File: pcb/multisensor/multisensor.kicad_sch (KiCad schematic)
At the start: 20 parts, among them J1 TTL_Serial, J2 mmWave_Data, J3 mmWave_Support, J4 PIR_Sensor, J5 BME680, J6 BH1750, J7 USB_B_Micro, Q1 PN2222A, Q2 PN2222A, SW1 RESET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

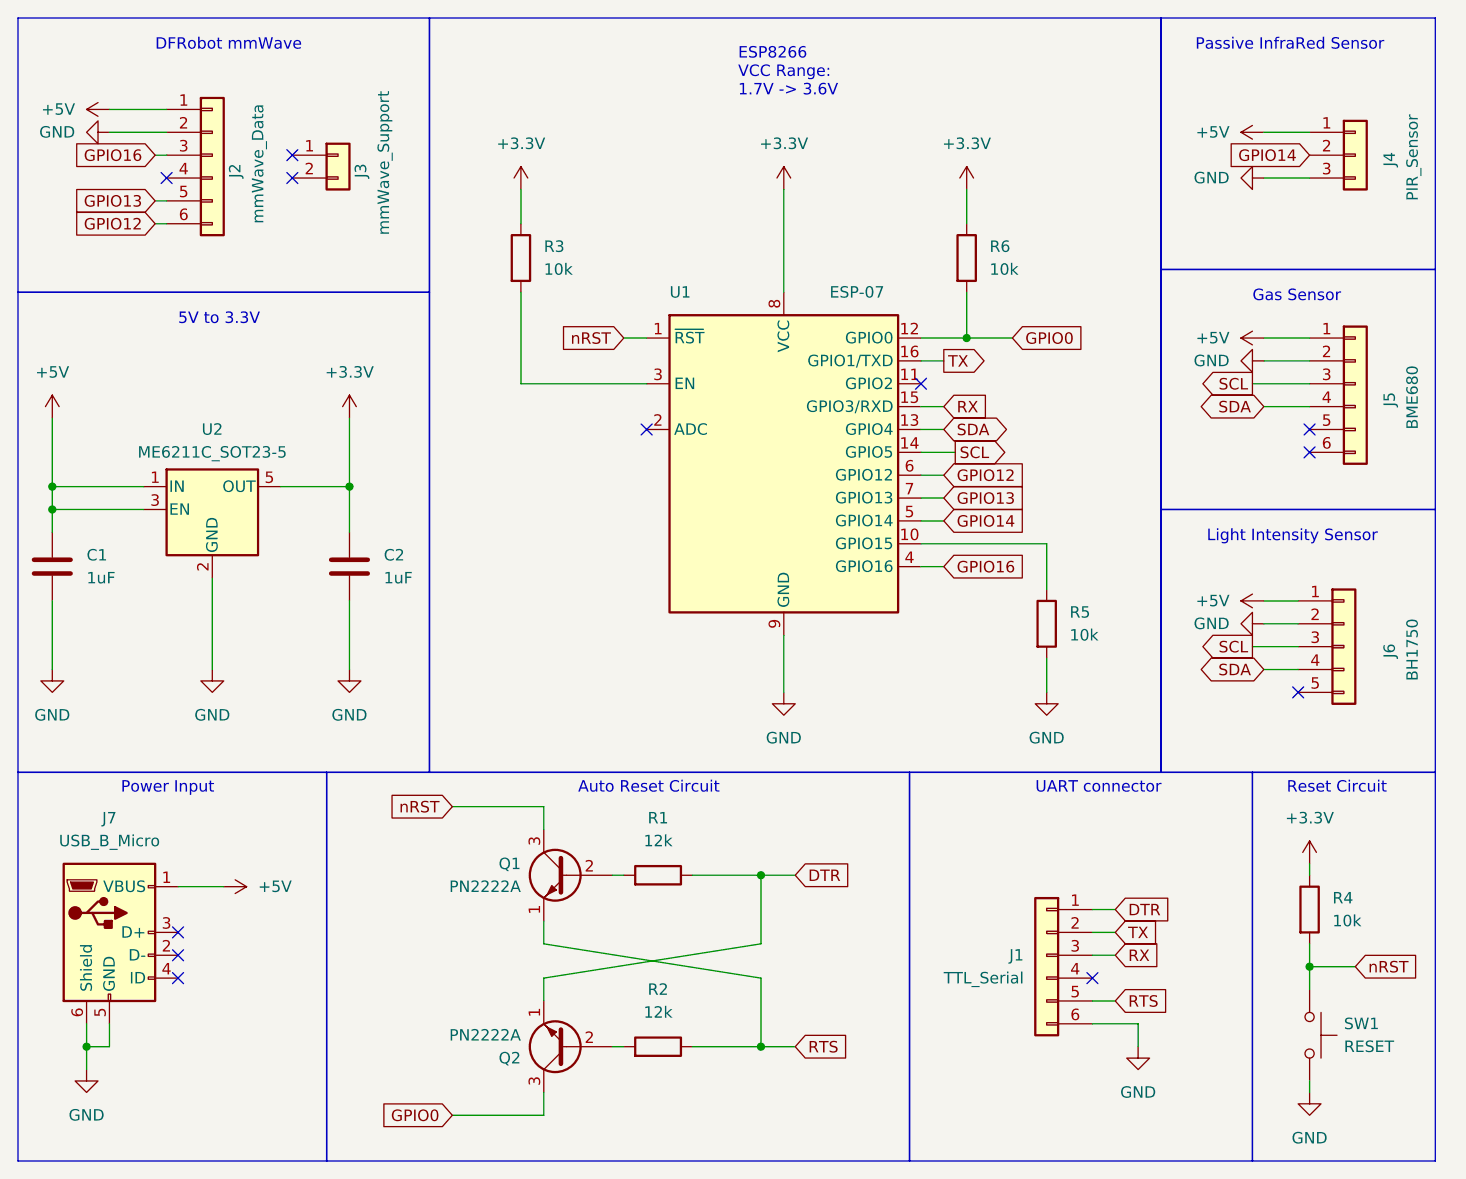
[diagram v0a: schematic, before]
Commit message: fix vcc/gnd pointing up/down
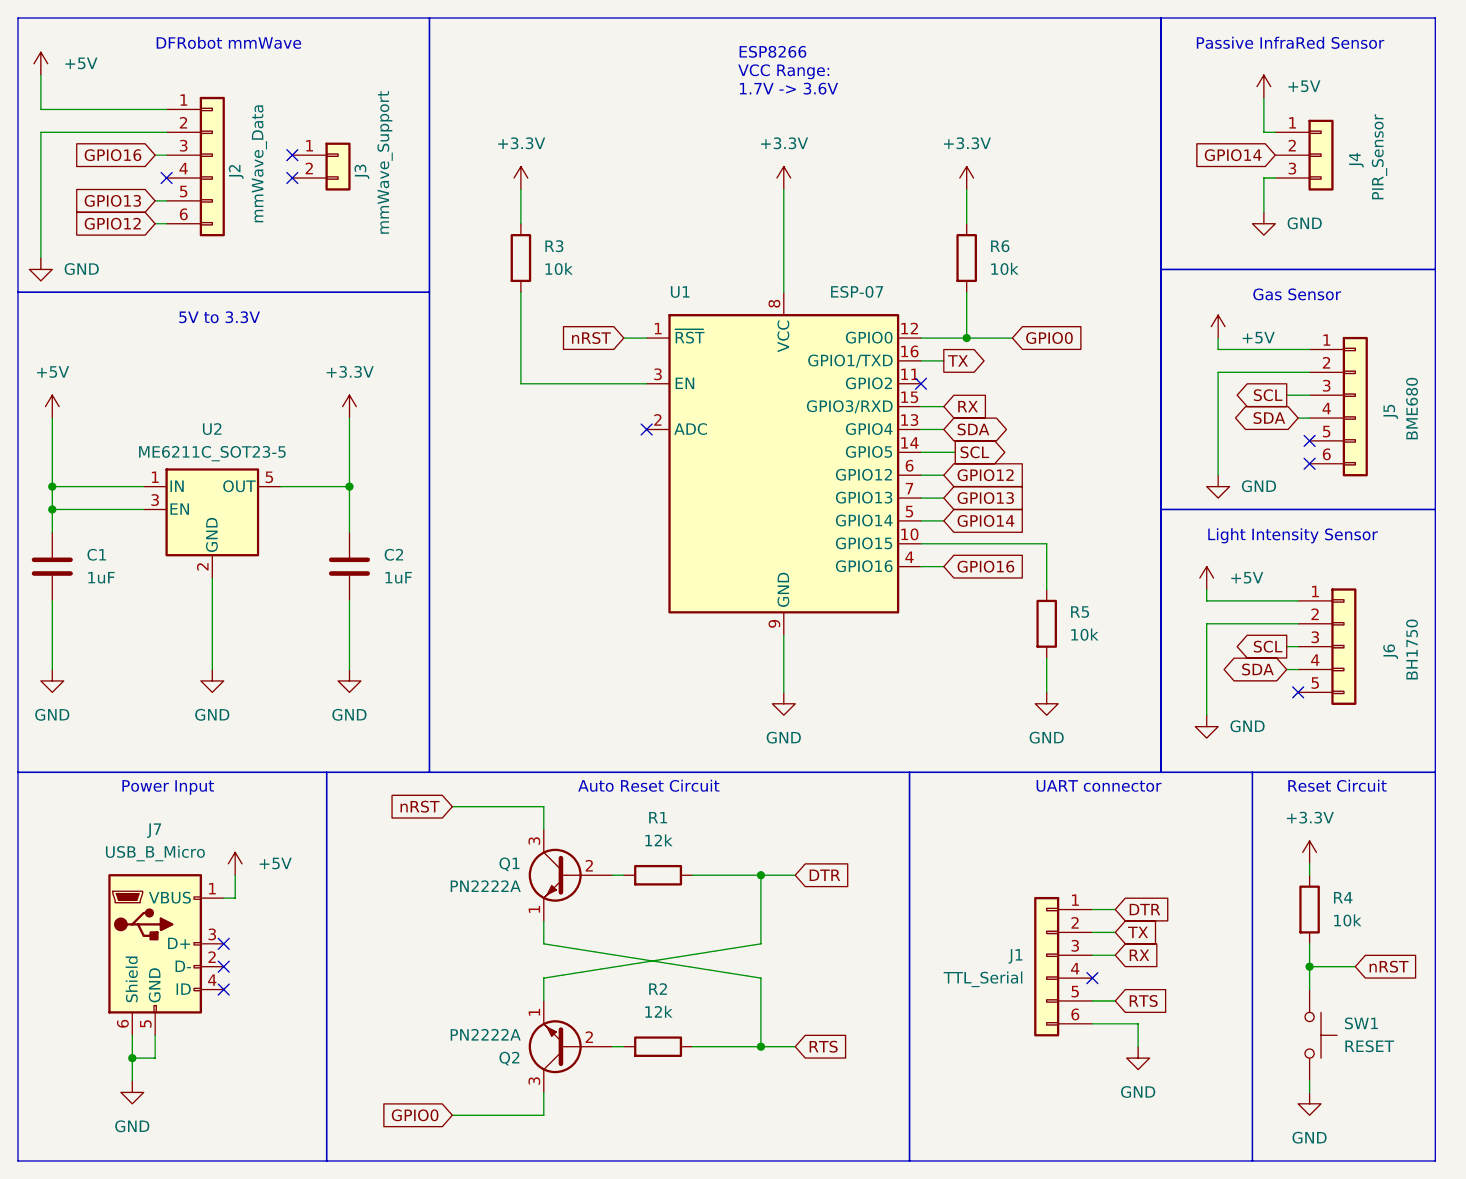
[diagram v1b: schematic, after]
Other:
- title: (none) -> Multisensor
- moved on the sheet: J4, J5, J7

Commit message: add tantalum caps to VCC
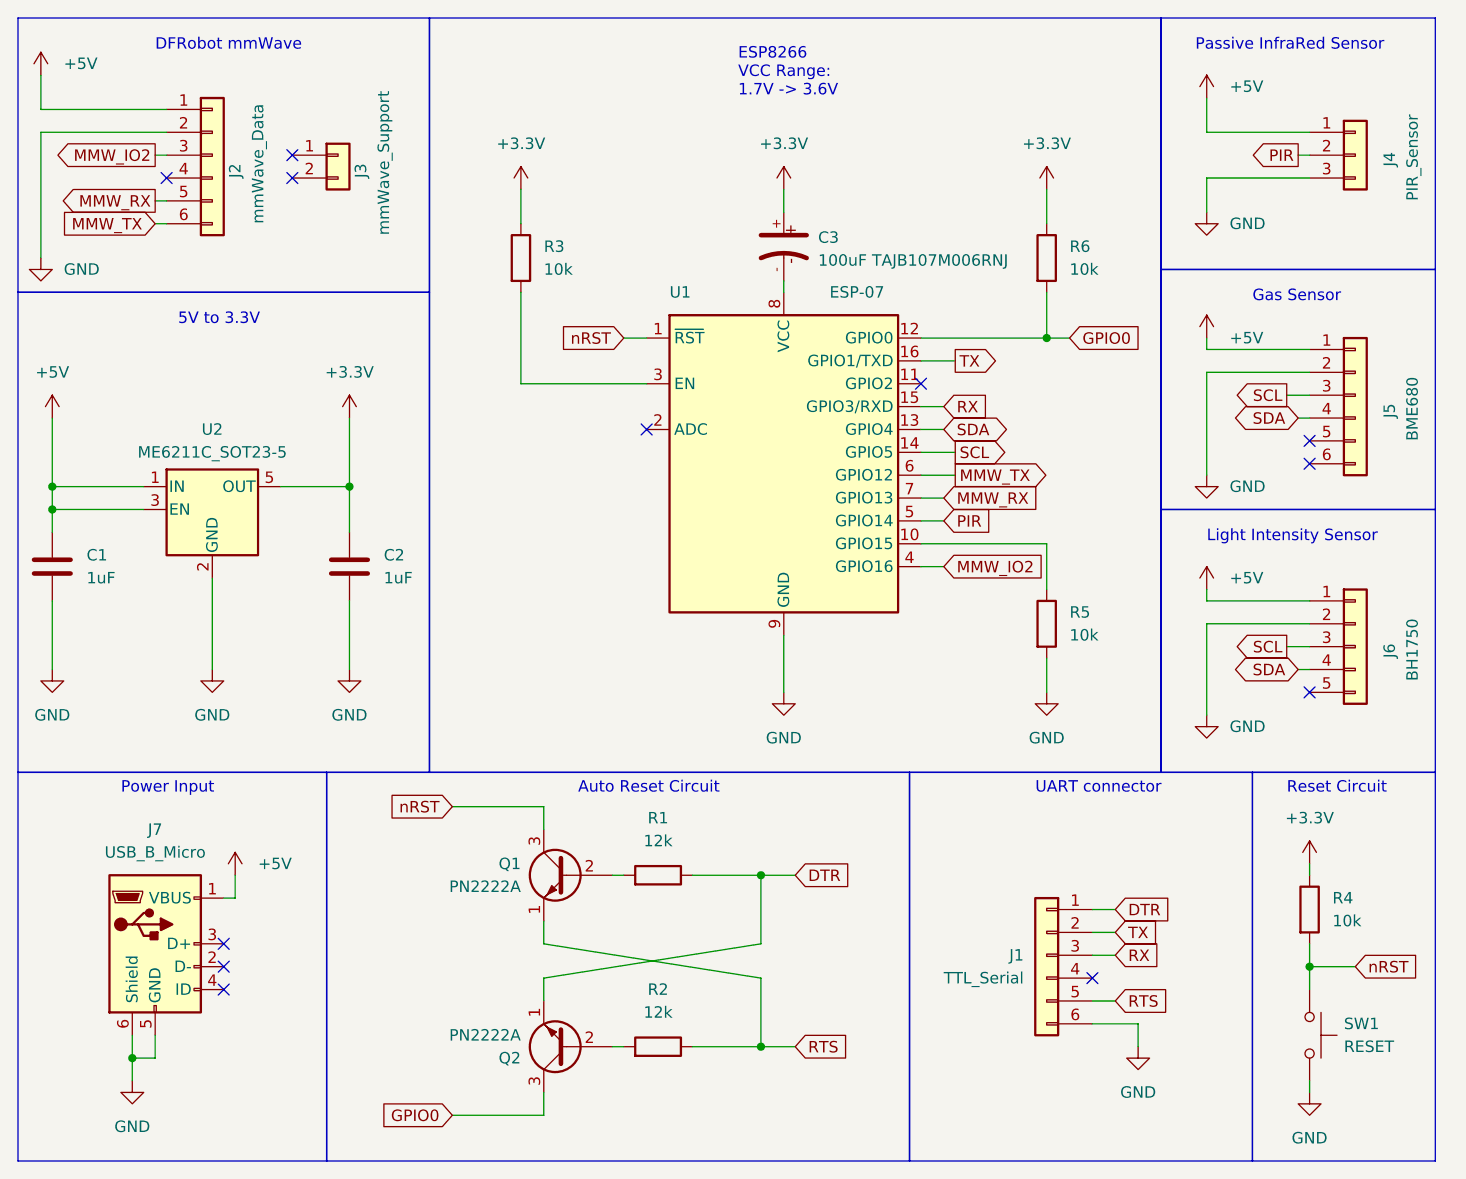
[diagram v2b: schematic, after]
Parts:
- added C3: 100uF TAJB107M006RNJ, *Multisensor:AVX-B, symbol TAJB107M006RNJ:TANTALUM-SMD-100UF-6.3V_AVX-B_
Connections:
- net +3.3V: now also C3.+; no longer U1.8 (VCC)
- net GPIO12 renamed MMW_TX
- net GPIO13 renamed MMW_RX
- net GPIO14 renamed PIR
- net GPIO16 renamed MMW_IO2
- new net: C3.-, U1.8 (VCC)
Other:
- moved on the sheet: J4, J6, R6

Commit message: add filtering caps + external pullups
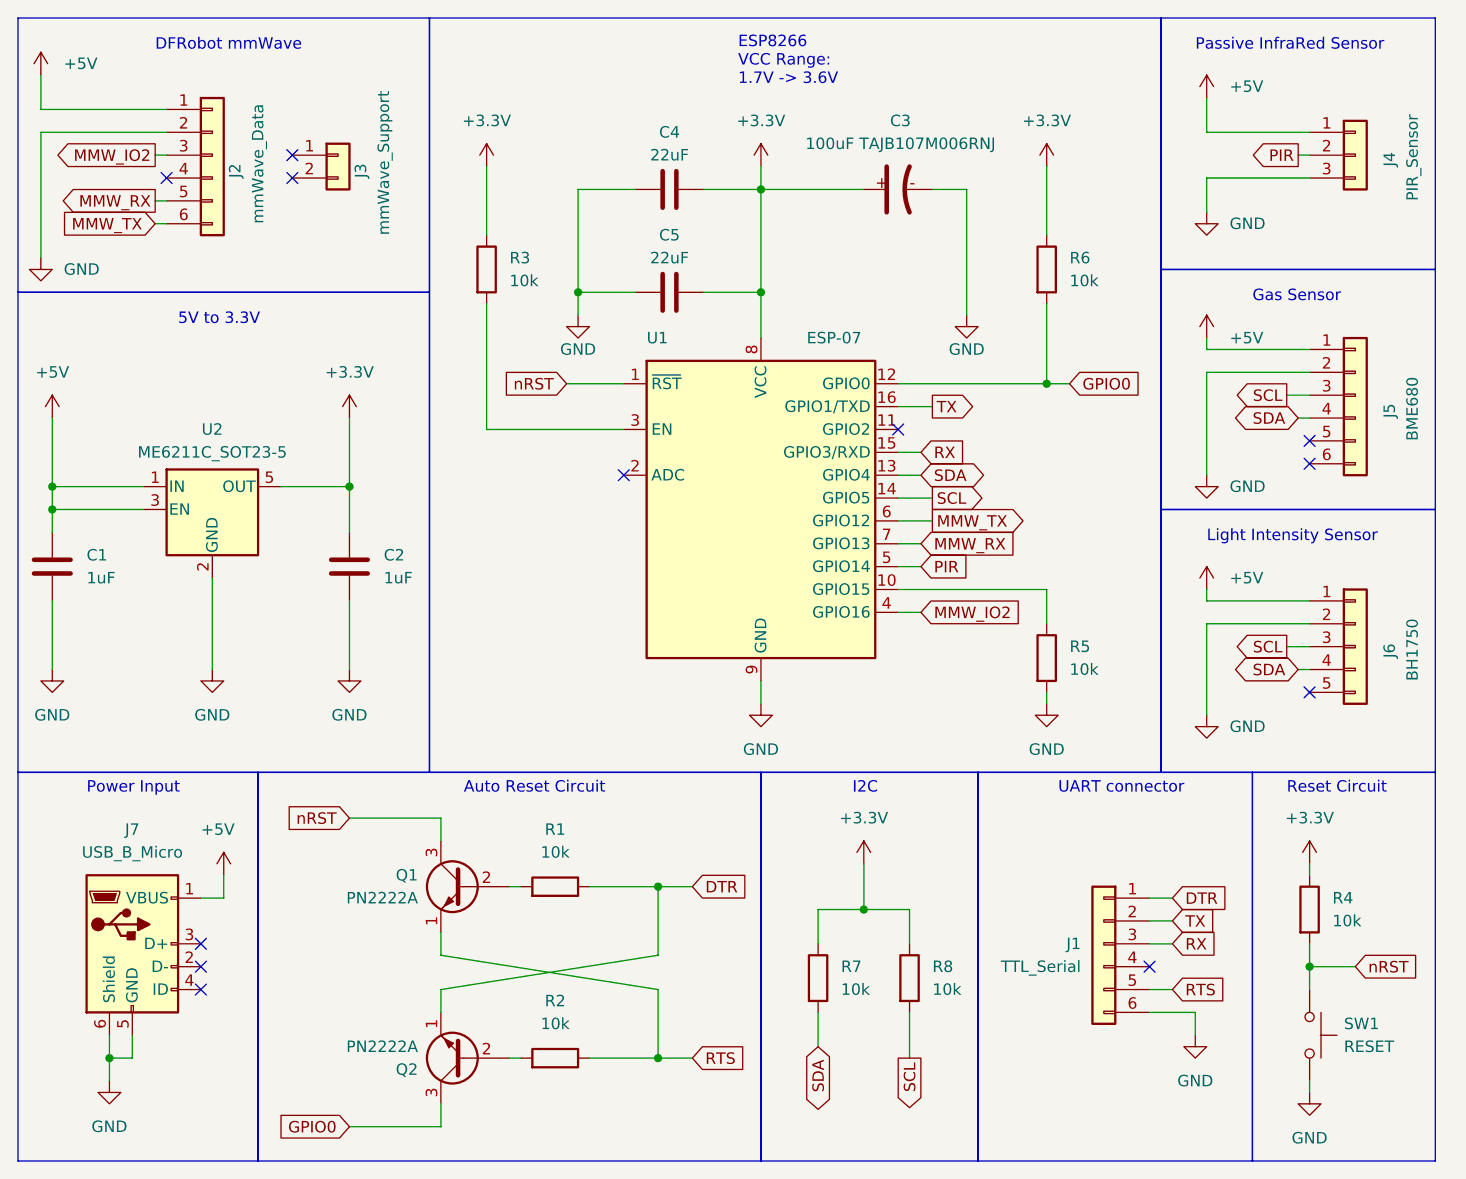
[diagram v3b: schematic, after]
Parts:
- added C4, C5: 22uF, Capacitor_SMD:C_1210_3225Metric, symbol Device:C
- added R7, R8: 10k, Resistor_SMD:R_0805_2012Metric, symbol Device:R
- R1, R2: value 12k -> 10k
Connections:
- net +3.3V: now also U1.8 (VCC), C4.2, C5.2, R7.1, R8.1
- net GND: now also C3.-, C4.1, C5.1
- net SCL: now also R8.2
- net SDA: now also R7.2
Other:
- note added: "I2C"
- moved on the sheet: J1, J7, Q1, Q2, R1, R2, R3, R5, R6, U1

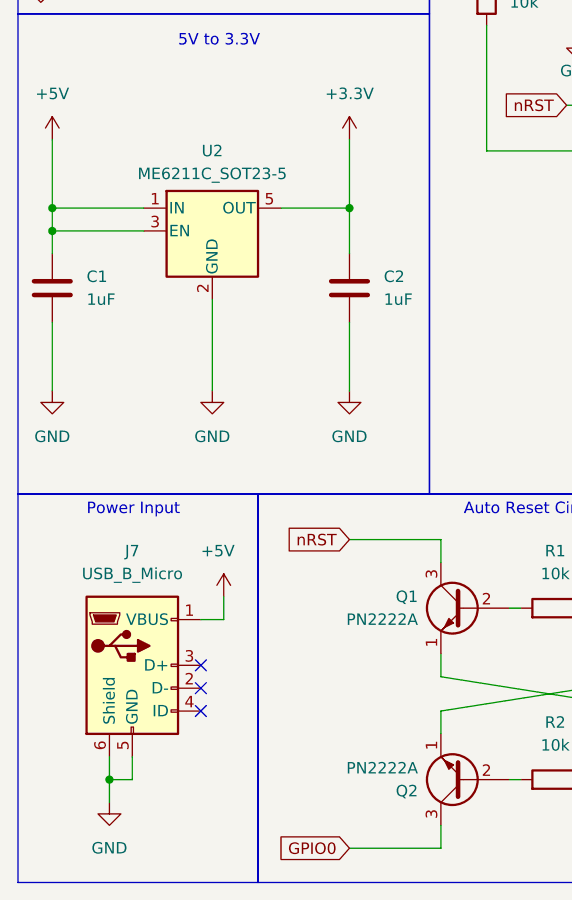
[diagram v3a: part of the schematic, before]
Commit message: upadate regulator and connector
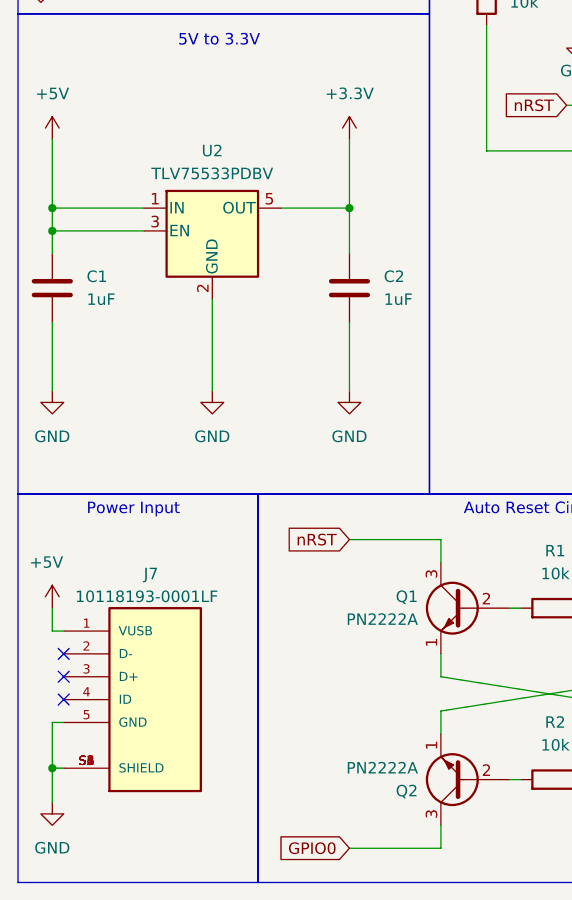
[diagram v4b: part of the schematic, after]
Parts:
- removed J7: USB_B_Micro, Connector_USB:USB_Micro-B_Amphenol_10103594-0001LF_Horizontal, symbol Connector:USB_B_Micro
- added J7: 10118193-0001LF, *Multisensor:AMPHENOL_10118193-0001LF, symbol 10118193-0001LF:10118193-0001LF
- C1, C2: footprint Capacitor_SMD:C_0805_2012Metric -> Capacitor_SMD:C_1206_3216Metric; MPN (none) -> NMC1206X7R105K50TRPLPF
- C4, C5: MPN (none) -> CL32A226MOJNNNE
- U2: value ME6211C_SOT23-5 -> TLV75533PDBV; symbol Regulator_Linear:TLV70233_SOT23-5 -> Regulator_Linear:TLV75533PDBV
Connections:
- net +5V: now also J7.1 (VUSB)
- net GND: now also J7.5 (GND), J7.S1 (SHIELD), J7.S2 (SHIELD), J7.S3 (SHIELD), J7.S4 (SHIELD), J7.S5 (SHIELD), J7.S6 (SHIELD)
